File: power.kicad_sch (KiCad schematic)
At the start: 32 parts, among them J1 Conn_01x02, U1 ZXCT1107, U2 ST715M25R

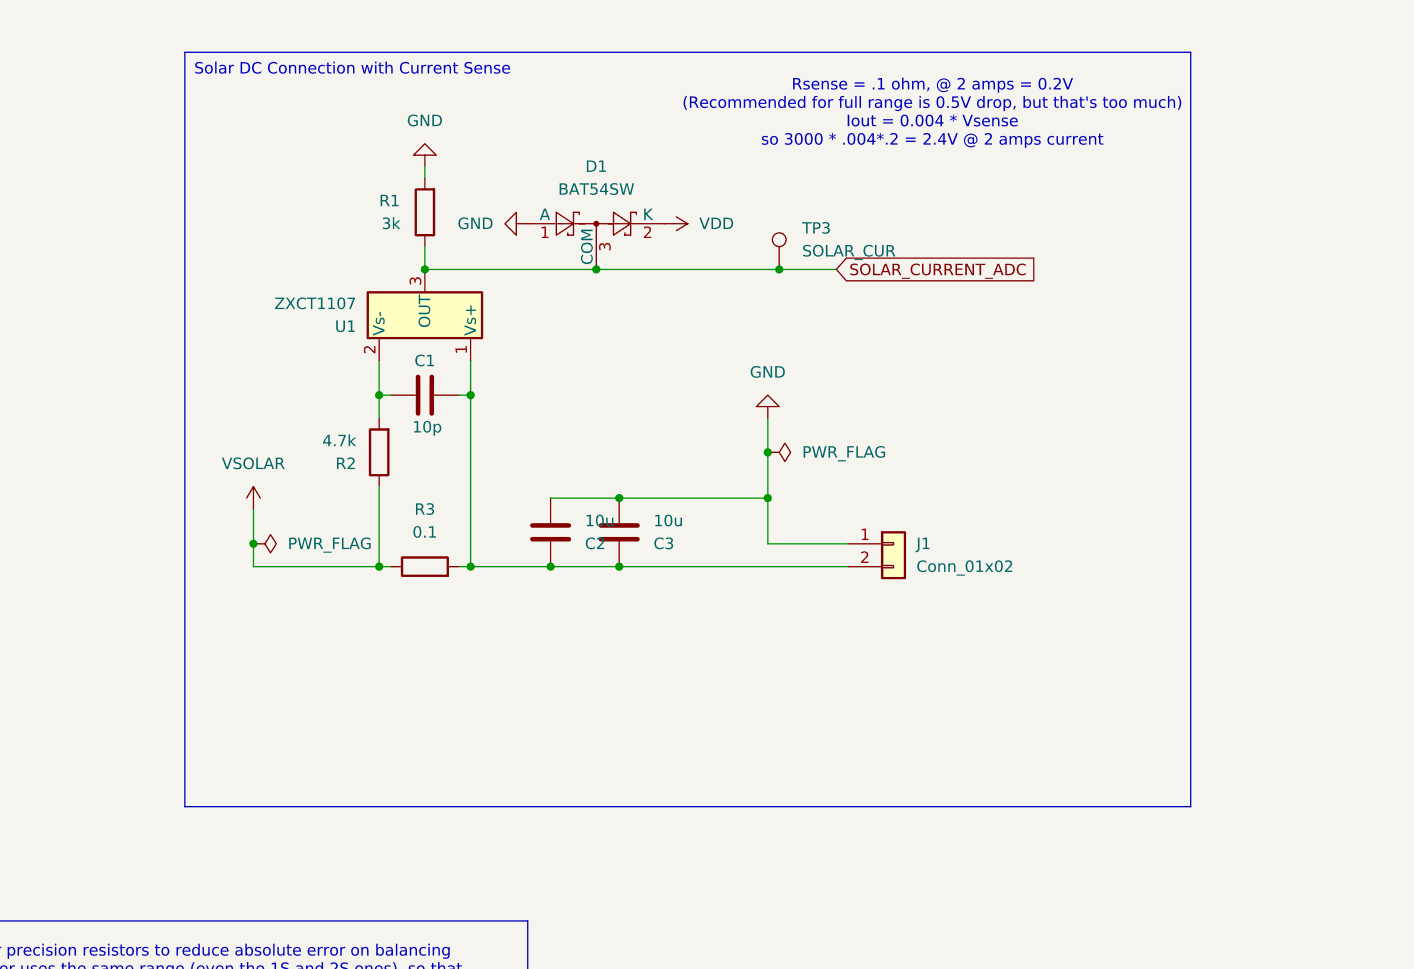
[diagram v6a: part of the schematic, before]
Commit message: Adding switch, moving current sense
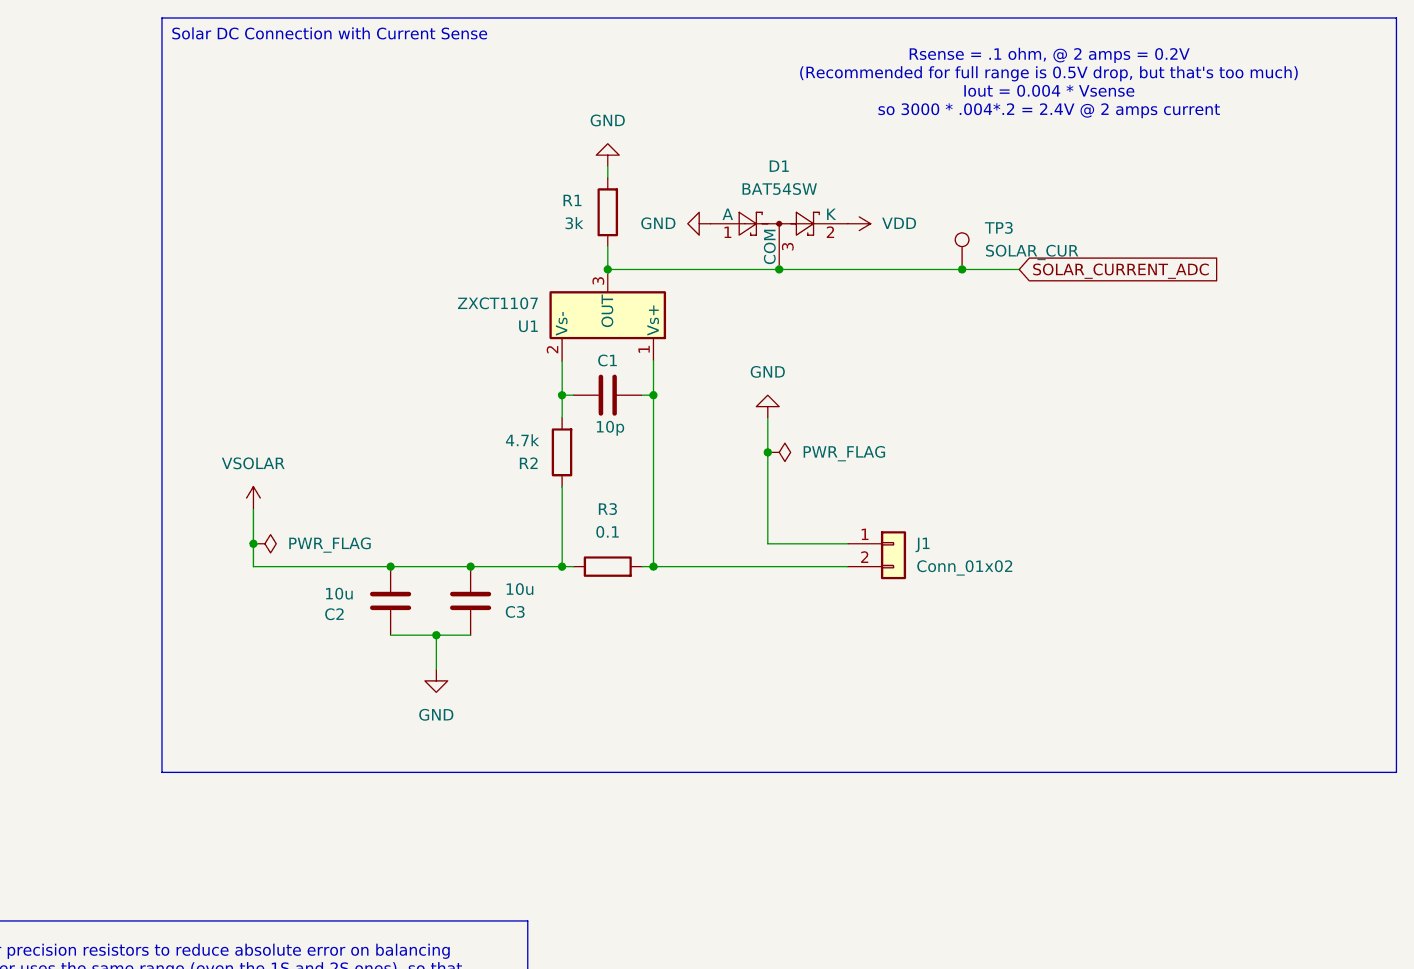
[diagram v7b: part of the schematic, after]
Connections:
- net GND: now also C2.1, C3.1; no longer C2.2, C3.2
- net VSOLAR: now also C2.2, C3.2
- net at C1.1, J1.2 (Pin_2), R3.2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: no longer C2.1, C3.1
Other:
- moved on the sheet: C1, C2, C3, D1, R1, R2, R3, TP3, U1

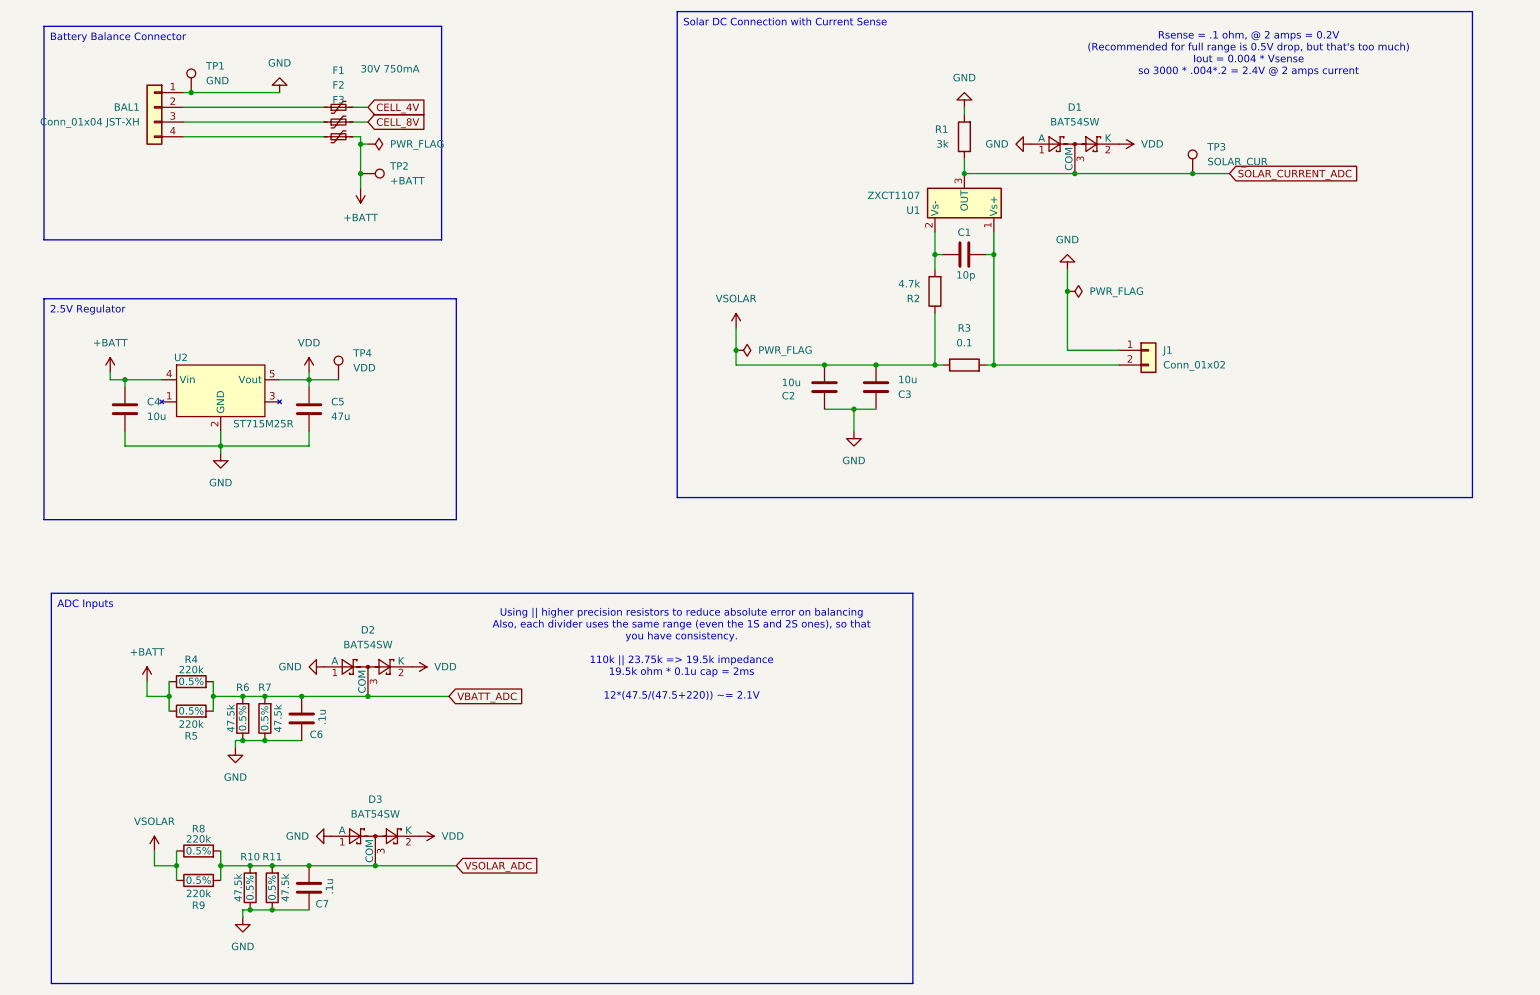
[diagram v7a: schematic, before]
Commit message: Starting draft of ADC multiplexer
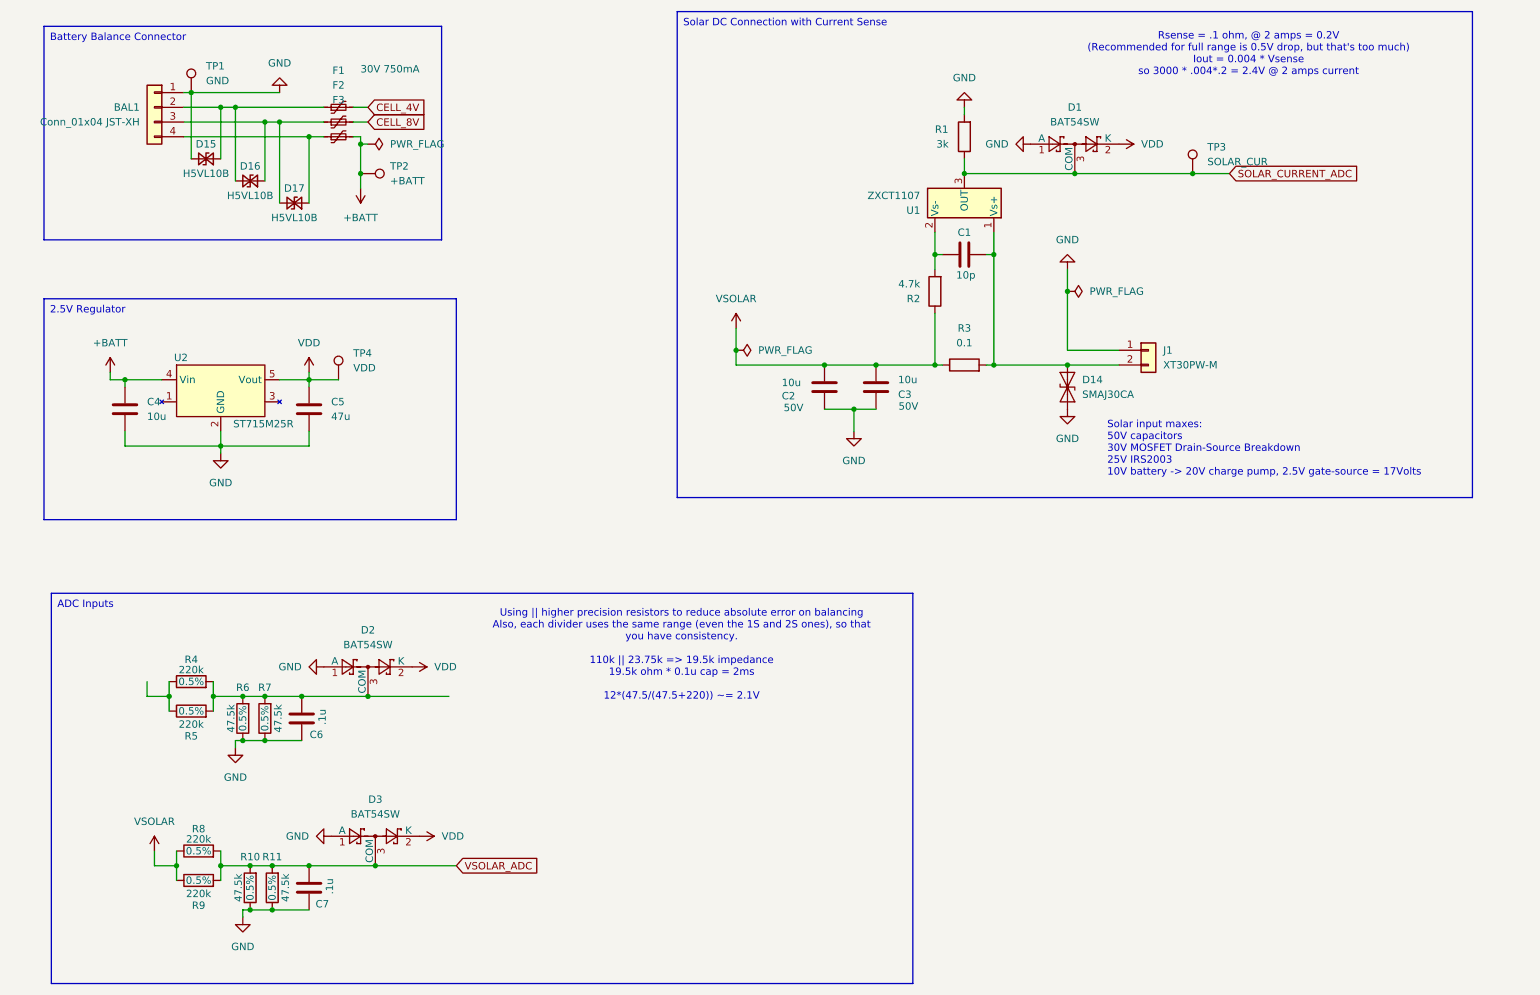
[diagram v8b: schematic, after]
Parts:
- added D14: SMAJ30CA, Diode_SMD:D_SMA, symbol Diode:SMAJ30CA
- added D15, D16, D17: H5VL10B, Diode_SMD:D_SOD-882, symbol Device:D_TVS_Small
- BAL1: footprint Connector_JST:JST_XH_S4B-XH-A_1x04_P2.50mm_Horizontal -> JakeLib:JST_XH_S4B-XH-A_1x04_P2.50mm_Horizontal_Tight
- C2, C3: Voltage (none) -> 50V
- J1: value Conn_01x02 -> XT30PW-M
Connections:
- net +BATT: no longer R4.1, R5.1
- net GND: now also D14.1 (A1), D15.2 (A2)
- net at BAL1.4 (Pin_4), F3.1: now also D17.1 (A1)
- net at BAL1.2 (Pin_2), F1.1: now also D15.1 (A1), D16.2 (A2)
- net at C1.1, J1.2 (Pin_2), R3.2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: now also D14.2 (A2)
- net at BAL1.3 (Pin_3), F2.1: now also D16.1 (A1), D17.2 (A2)
- net VBATT_ADC: no longer names the net of C6.1, D2.3 (COM), R4.2, R5.2, R6.2, R7.2
- new net: R4.1, R5.1
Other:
- note added: "Solar input maxes: 50V capacitors 30V MOSFET Drain-Source Breakdown 25V IRS2003 10V battery -> 20V charge pump, 2.5V gate-source = 17Volts"
